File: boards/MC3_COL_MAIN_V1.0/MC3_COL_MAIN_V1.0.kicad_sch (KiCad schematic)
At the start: 0 parts

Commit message: Schematic WIP: Power, MCU, Connectors, MotorChannel sheets wired; root hierarchy with 4 channel instances
All nets per the vault Main-Board-01 pages (MCU Pinout, Motor Channel, Encoder Interface,
Connectors, BOM). Custom fields COTS/LCSC/MPN/Note on instances. Provisional choices marked.
Root sheet pins not yet wired.

Co-Authored-By: Claude Fable 5 <noreply@anthropic.com>
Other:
- added sheet Connectors (Connectors.kicad_sch)
- added sheet MCU (MCU.kicad_sch)
- added sheet Power (Power.kicad_sch)
- added sheet leaf1 (MotorChannel.kicad_sch)
- added sheet leaf2 (MotorChannel.kicad_sch)
- added sheet leaf3 (MotorChannel.kicad_sch)
- added sheet leaf4 (MotorChannel.kicad_sch)

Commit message: Schematic: root sheet on-grid, I2C address straps as GND/+3V3 global labels, ERC clean (warnings only)
- Root: Power/MCU/Connectors + 4x MotorChannel instances on the 1.27 mm grid; sheet pins wired
  to EN/PH/IPROPI/RC_OUT/nFAULT_leafN global labels; A1/A0 straps leaf1 GND/GND, leaf2
  GND/+3V3, leaf3 +3V3/GND, leaf4 +3V3/+3V3 (PROVISIONAL)
- Connectors: removed a GND drop that shorted ENC_leaf4; VM on the FFCs as global labels
- Power: PWR_FLAGs placed on the pin ends (VIN_PROT, VM, GND)
- ERC (kicad-cli, all severities): 0 errors, 8 same_local_global_label warnings (intended)
- Reference designators still duplicated across the 4 channel instances: needs Annotate
  in eeschema (no CLI path)

Co-Authored-By: Claude Fable 5 <noreply@anthropic.com>
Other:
- note added: "MC3_COL_MAIN_V1.0 - MC3 collimator main control board. Vault build rung: Projects/MC3 Collimator/05 Builds/Main-Board-01. Four leaf channels fitted (DRV8214, COL-COTS-0028); yaw reserved at the MCU only. A1/A0 I2C address straps per leaf: leaf1 GND/GND, leaf2 GND/+3V3, leaf3 +3V3/GND, leaf4 +3V3/+3V3 (PROVISIONAL). Net naming: vault V3_3 == +3V3, vault VIN_RAW == VM."

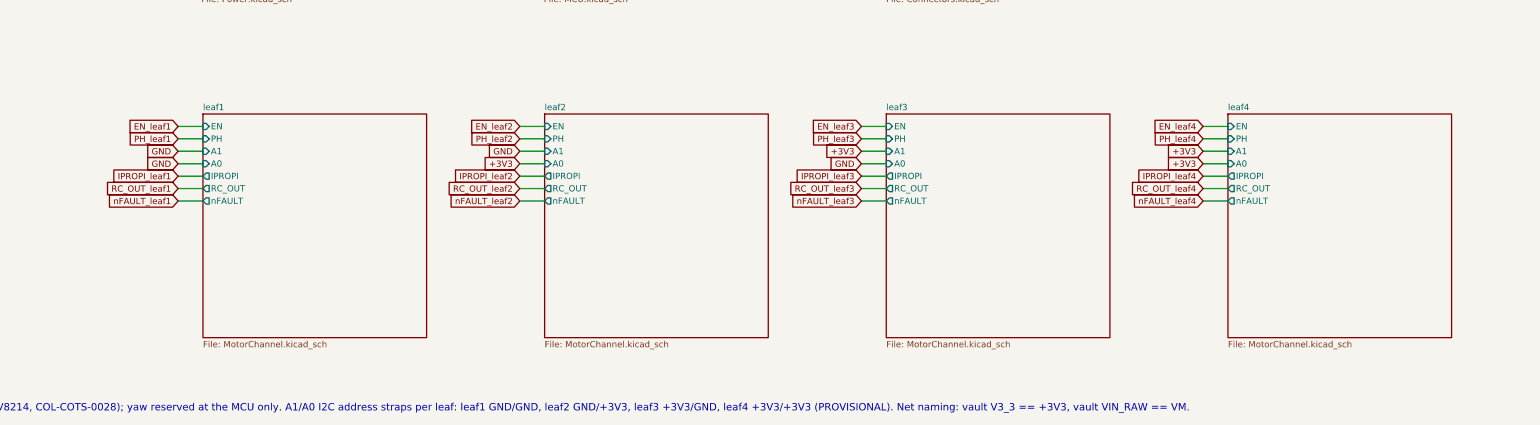
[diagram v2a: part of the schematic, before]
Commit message: Schematic annotated in eeschema (per-instance references for the 4 channel sheets); user review OK
Co-Authored-By: Claude Fable 5 <noreply@anthropic.com>
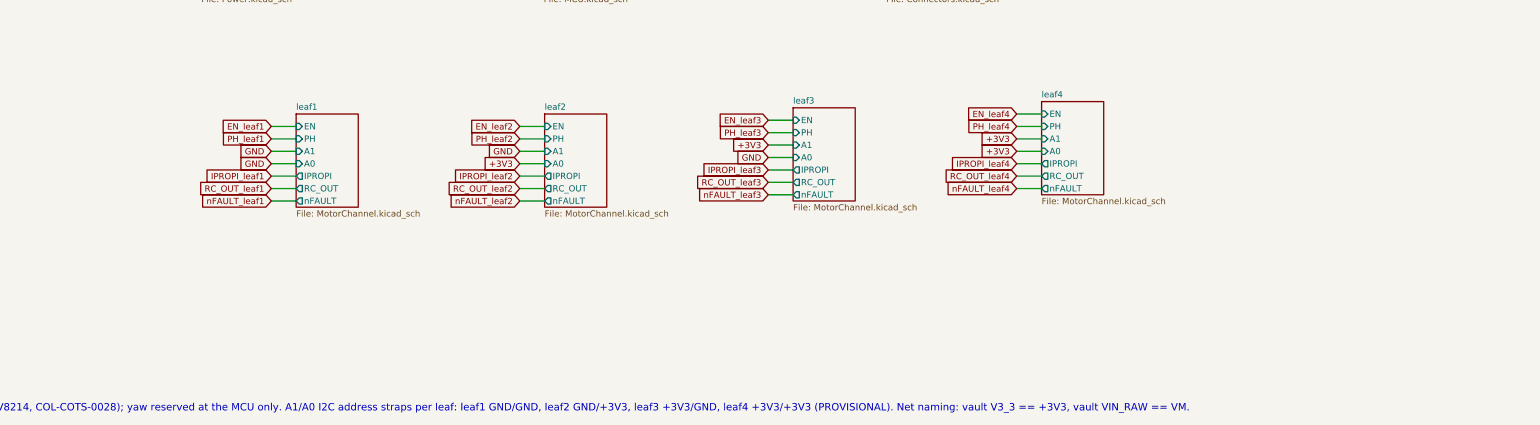
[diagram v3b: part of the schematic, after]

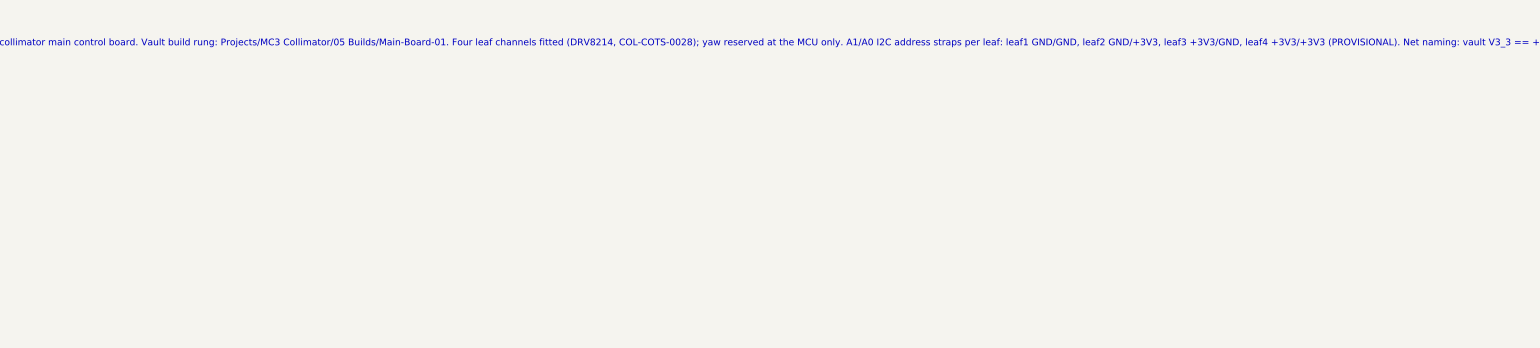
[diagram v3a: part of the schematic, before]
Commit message: Remove tscircuit entirely: sources, imports, skills, Node tooling, snapshots; KiCad is the only design tool
Deleted: boards/MC3_COL_MAIN_V1.0/*.tsx|*.ts|tests/, imports/, scripts/, index/postest
.circuit.tsx, manual-edits.json, tscircuit.config.json, tsconfig.json, package.json, bun.lock,
.npmrc, __snapshots__/, .claude/skills/tscircuit/, .agents/skills/tscircuit/ (plus untracked
node_modules/, .tscircuit/, dist/). .gitignore reduced to KiCad/Konnect/IDE entries.
CLAUDE.md banner replaced by a history note; docs/design/parts/STM32F411.md rewritten for the
KiCad schematic.

Co-Authored-By: Claude Fable 5 <noreply@anthropic.com>
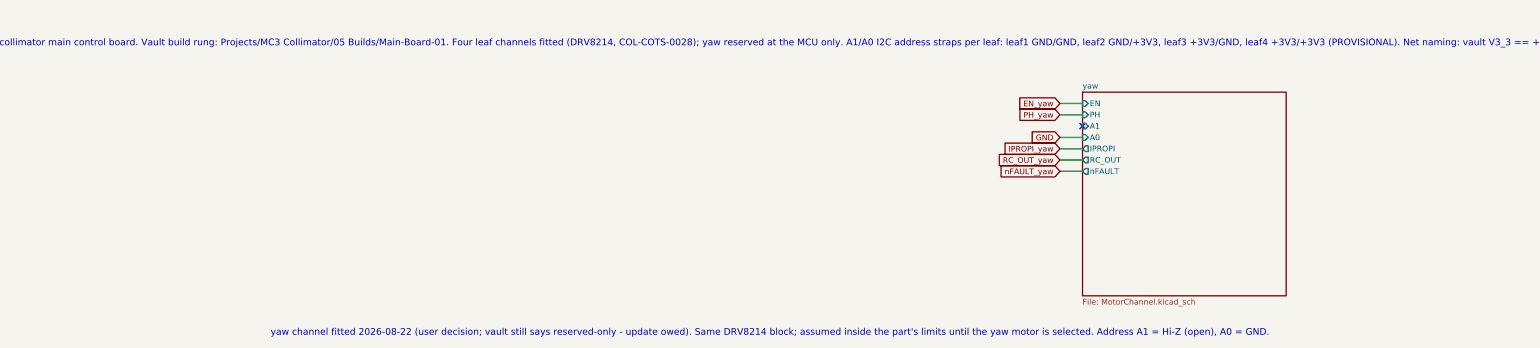
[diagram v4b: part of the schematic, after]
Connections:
- no-connect marks 0 -> 1
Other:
- added sheet yaw (MotorChannel.kicad_sch)
- note added: "yaw channel fitted 2026-08-22 (user decision; vault still says reserved-only - update owed). Same DRV8214 block; assumed inside the part's limits until the yaw motor is selected. Address A1 = Hi-Z (open), A0 = GND."

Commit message: I2C address straps: high straps via 2.2k pull-ups R40-R43 (SLVSH04 Table 8-28 note); address table on root sheet
Co-Authored-By: Claude Fable 5 <noreply@anthropic.com>
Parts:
- added R40, R41, R42, R43: 2.2k, MC3_COL_MAIN:R_0402_1005Metric, symbol Device:R
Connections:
- net +3V3: now also R40.1, R41.1, R42.1, R43.1
- new net leaf2/A0: R40.2
- new net leaf3/A1: R41.2
- new net leaf4/A0: R43.2
- new net leaf4/A1: R42.2
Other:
- note added: "Address straps per SLVSH04 Table 8-28: leaf1 0/0 -> 0x60, leaf2 0/1 -> 0x64, leaf3 1/0 -> 0x6C, leaf4 1/1 -> 0x70, yaw Z/0 -> 0x66 (write addresses). High straps via 2.2k per TI; low straps tied to GND; Hi-Z left open."

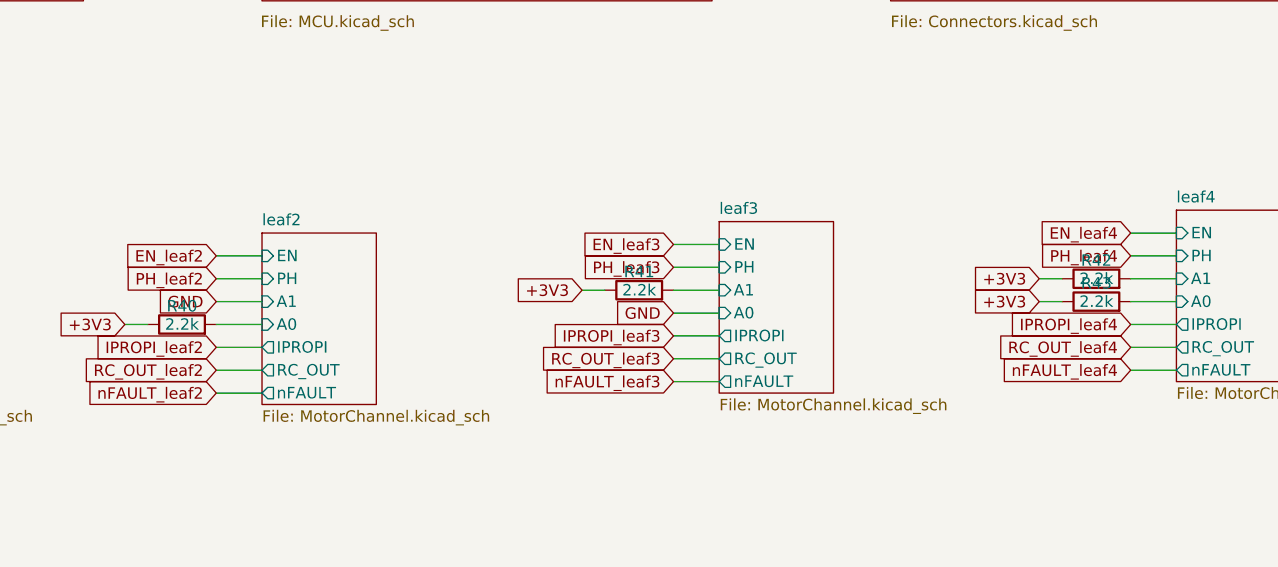
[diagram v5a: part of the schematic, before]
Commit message: Schematic re-annotated in eeschema after yaw channel + strap pull-ups
Co-Authored-By: Claude Fable 5 <noreply@anthropic.com>
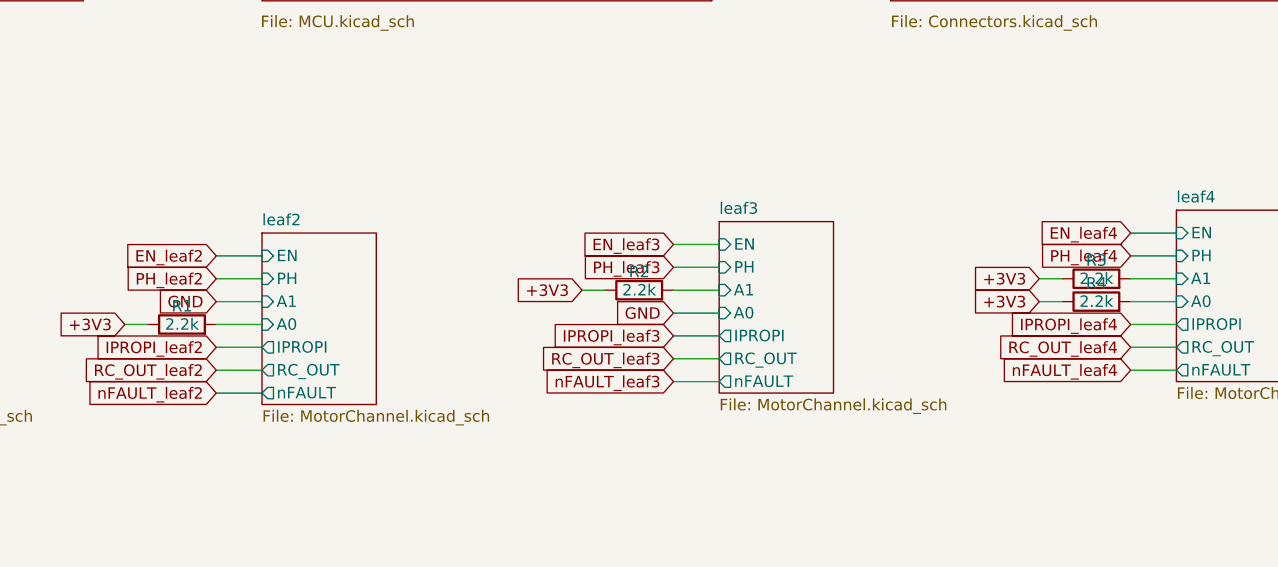
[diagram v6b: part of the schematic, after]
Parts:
- renumbered R40 to R1, R41 to R2, R42 to R3, R43 to R4

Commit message: LCSC/MPN fields on every support part (verified against the JLCPCB DB); R_IPROPI 6.8k = C93940; polyfuse 1206L200/12NR; MIGRATION register
Co-Authored-By: Claude Fable 5 <noreply@anthropic.com>
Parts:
- R1, R2, R3, R4: LCSC (none) -> C25879; MPN (none) -> 0402WGF2201TCE
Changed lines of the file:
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@@
 			)
 		)
-	)
+		(property "LCSC" "C25879"
+			(at 182.88 77.47 0)
+			(hide yes)
+			(effects
+				(font
+					(size 1.27 1.27)
+				)
+			)
+		)
+		(property "MPN" "0402WGF2201TCE"
+			(at 182.88 77.47 0)
+			(hide yes)
+			(effects
+				(font
+					(size 1.27 1.27)
+				)
+			)
+		))
 	(symbol
 		(lib_id "Device:R")
@@
 			)
 		)
-	)
+		(property "LCSC" "C25879"
+			(at 132.08 76.2 0)
+			(hide yes)
+			(effects
+				(font
+					(size 1.27 1.27)
+				)
+			)
+		)
+		(property "MPN" "0402WGF2201TCE"
+			(at 132.08 76.2 0)
+			(hide yes)
+			(effects
+				(font
+					(size 1.27 1.27)
+				)
+			)
+		))
 	(symbol
 		(lib_id "Device:R")
@@
 			)
 		)
-	)
+		(property "LCSC" "C25879"
+			(at 182.88 74.93 0)
+			(hide yes)
+			(effects
+				(font
+					(size 1.27 1.27)
+				)
+			)
+		)
+		(property "MPN" "0402WGF2201TCE"
+			(at 182.88 74.93 0)
+			(hide yes)
+			(effects
+				(font
+					(size 1.27 1.27)
+				)
+			)
+		))
 	(symbol
 		(lib_id "Device:R")
@@
 			)
 		)
-	)
+		(property "LCSC" "C25879"
+			(at 81.28 80.01 0)
+			(hide yes)
+			(effects
+				(font
+					(size 1.27 1.27)
+				)
+			)
+		)
+		(property "MPN" "0402WGF2201TCE"
+			(at 81.28 80.01 0)
+			(hide yes)
+			(effects
+				(font
+					(size 1.27 1.27)
+				)
+			)
+		))
 	(sheet
 		(at 90.17 69.85)

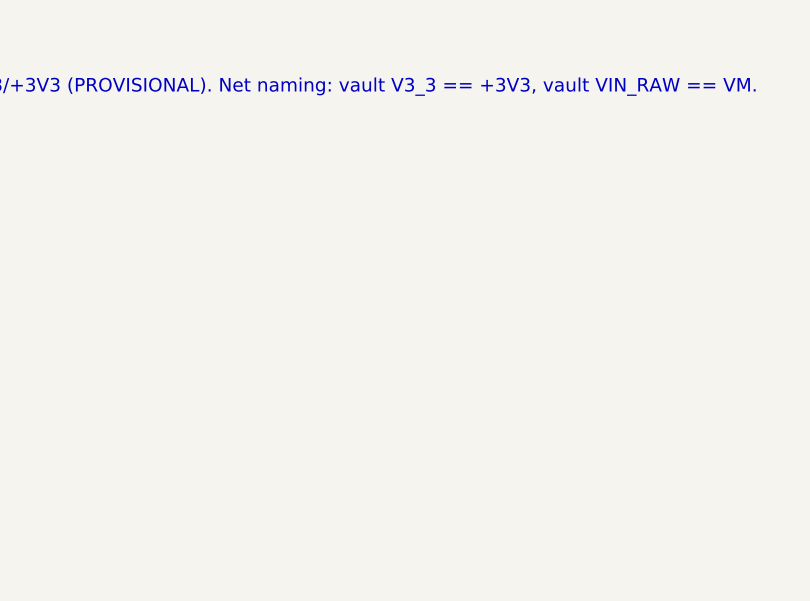
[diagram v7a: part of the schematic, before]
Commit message: MCU -> STM32F412RET6 (pin-identical, adds bxCAN); CAN sheet: TJA1051T/3, split termination + jumper, PESD1CAN, CANH/CANL/GND pads
- MCU: U2 symbol MC3_COL_MAIN:STM32F412RET6 (same pin map as the F411), LCSC C89374; CAN1_RX PA11,
  CAN1_TX PA12; RC_OUT_leaf4 moved PA11 -> PB14
- CAN.kicad_sch (root sheet 'CAN'): U70 TJA1051T/3 (C38695) VCC from VM via FB62 + C70/C71,
  VIO +3V3, S low; JP70 solder jumper (bridged) -> R70/R71 62R split termination with C72 4.7nF;
  D70 PESD1CAN (C15771); J70 3 bare pads CANH/CANL/GND (new footprint SolderPads_3x)
- Library: STM32F412RET6 symbol; SolderPads_3x_2.2x1.4mm_P2.6mm, SOT-23, SolderJumper-2 footprints
- ERC 0 errors; netlist checked

Co-Authored-By: Claude Fable 5 <noreply@anthropic.com>
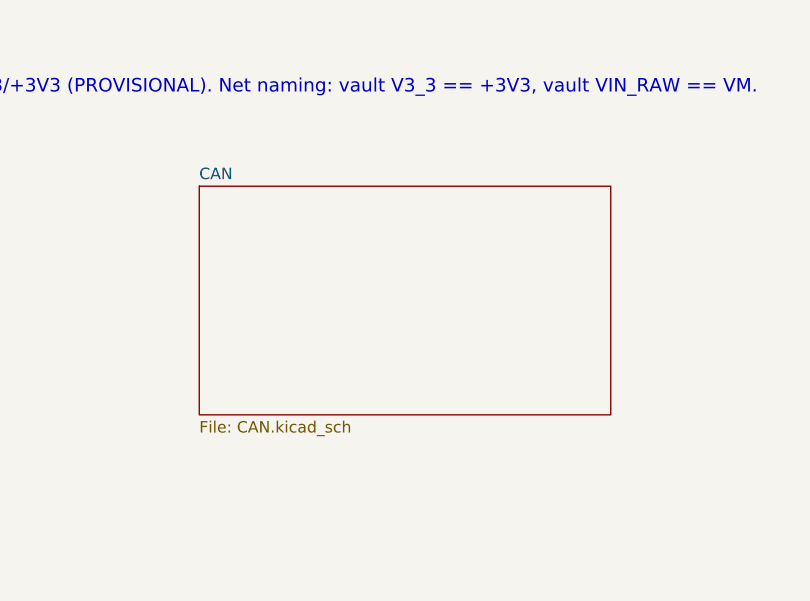
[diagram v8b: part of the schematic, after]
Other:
- added sheet CAN (CAN.kicad_sch)
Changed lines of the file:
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@@
+			)
+		)
+		(property "LCSC" "C25879"
+			(at 182.88 77.47 0)
+			(hide yes)
+			(show_name no)
+			(do_not_autoplace no)
+			(effects
+				(font
+					(size 1.27 1.27)
+				)
+			)
+		)
+		(property "MPN" "0402WGF2201TCE"
+			(at 182.88 77.47 0)
+			(hide yes)
+			(show_name no)
+			(do_not_autoplace no)
+			(effects
+				(font
+					(size 1.27 1.27)
+				)
 			)
 		)
@@
 			)
 		)
-		(property "LCSC" "C25879"
-			(at 182.88 77.47 0)
-			(hide yes)
-			(effects
-				(font
-					(size 1.27 1.27)
-				)
-			)
-		)
-		(property "MPN" "0402WGF2201TCE"
-			(at 182.88 77.47 0)
-			(hide yes)
-			(effects
-				(font
-					(size 1.27 1.27)
-				)
-			)
-		))
+	)
 	(symbol
 		(lib_id "Device:R")
@@
 			)
 		)
+		(property "LCSC" "C25879"
+			(at 132.08 76.2 0)
+			(hide yes)
+			(show_name no)
+			(do_not_autoplace no)
+			(effects
+				(font
+					(size 1.27 1.27)
+				)
+			)
+		)
+		(property "MPN" "0402WGF2201TCE"
+			(at 132.08 76.2 0)
+			(hide yes)
+			(show_name no)
+			(do_not_autoplace no)
+			(effects
+				(font
+					(size 1.27 1.27)
+				)
+			)
+		)
 		(pin "2"
 		)
@@
 			)
 		)
-		(property "LCSC" "C25879"
-			(at 132.08 76.2 0)
-			(hide yes)
-			(effects
-				(font
-					(size 1.27 1.27)
-				)
-			)
-		)
-		(property "MPN" "0402WGF2201TCE"
-			(at 132.08 76.2 0)
-			(hide yes)
-			(effects
-				(font
-					(size 1.27 1.27)
-				)
-			)
-		))
+	)
 	(symbol
 		(lib_id "Device:R")
@@
 			)
 		)
+		(property "LCSC" "C25879"
+			(at 182.88 74.93 0)
+			(hide yes)
+			(show_name no)
+			(do_not_autoplace no)
+			(effects
+				(font
+					(size 1.27 1.27)
+				)
+			)
+		)
+		(property "MPN" "0402WGF2201TCE"
+			(at 182.88 74.93 0)
+			(hide yes)
+			(show_name no)
+			(do_not_autoplace no)
+			(effects
+				(font
+					(size 1.27 1.27)
+				)
+			)
+		)
 		(pin "2"
 		)
@@
 			)
 		)
-		(property "LCSC" "C25879"
-			(at 182.88 74.93 0)
-			(hide yes)
-			(effects
-				(font
-					(size 1.27 1.27)
-				)
-			)
-		)
-		(property "MPN" "0402WGF2201TCE"
-			(at 182.88 74.93 0)
-			(hide yes)
-			(effects
-				(font
-					(size 1.27 1.27)
-				)
-			)
-		))
+	)
 	(symbol
 		(lib_id "Device:R")
@@
 			)
 		)
+		(property "LCSC" "C25879"
+			(at 81.28 80.01 0)
+			(hide yes)
+			(show_name no)
+			(do_not_autoplace no)
+			(effects
+				(font
+					(size 1.27 1.27)
+				)
+			)
+		)
+		(property "MPN" "0402WGF2201TCE"
+			(at 81.28 80.01 0)
+			(hide yes)
+			(show_name no)
+			(do_not_autoplace no)
+			(effects
+				(font
+					(size 1.27 1.27)
+				)
+			)
+		)
 		(pin "2"
 		)
@@
 			)
 		)
-		(property "LCSC" "C25879"
-			(at 81.28 80.01 0)
-			(hide yes)
-			(effects
-				(font
-					(size 1.27 1.27)
-				)
-			)
-		)
-		(property "MPN" "0402WGF2201TCE"
-			(at 81.28 80.01 0)
-			(hide yes)
-			(effects
-				(font
-					(size 1.27 1.27)
-				)
-			)
-		))
+	)
 	(sheet
 		(at 90.17 69.85)
@@
 		)
 	)
+	(sheet
+    (at 160.02 140.97)
+    (size 45.72 25.4)
+    (fields_autoplaced yes)
+    (stroke (width 0.1524) (type solid))
+    (fill (color 0 0 0 0.0))
+    (property "Sheetname" "CAN"
+      (at 160.02 140.335 0)
+      (effects (font (size 1.27 1.27)) (justify left bottom))
+    )
+    (property "Sheetfile" "CAN.kicad_sch"
+      (at 160.02 167.005 0)
+      (effects (font (size 1.27 1.27)) (justify left top))
+    )
+    (instances
+      (project "MC3_COL_MAIN_V1.0"
+        (path "/7d5f4202-d55e-4c7b-a2df-dd599db38e48" (page "10"))
+      )
+    )
+  )
 	(sheet_instances
 		(path "/"
